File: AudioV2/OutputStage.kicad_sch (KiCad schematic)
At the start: 6 parts, among them K1 DEST LINE, K2 DEST PHONE, K3 DEST MUTE, U1 ULN spare/TODO

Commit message: AudioV2: embed lib_symbols on all child schematics (KiCad 10)
ControlPanel, RelayBoard, and OutputStage had empty lib_symbols and
legacy symbol_inst without pin UUIDs — same pads-only issue as PowerModule.

- Extend sch_helpers: SYMBOL_SOURCES aliases, auto pin_numbers_for,
  BP5293 from Audio/, sanitize (type solid), sub-symbol rename on alias
- Regenerate all sheets via wire_circuit_design.py (power/control/relay/output)
- Fix Pico lib_id to MCU_Module:RaspberryPi_Pico (KiCad 10 name)
- SSD1306-128x64 embeds ER_OLEDM0.91 graphic under alias name
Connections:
- new net: K1.3, K2.10
- new net: K2.3, K3.10
- new net: K1.7, K3.1
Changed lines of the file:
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@@
 		(at 88.9 50.8 0)
 		(unit 1)
+		(body_style 1)
 		(exclude_from_sim no)
 		(in_bom yes)
 		(on_board yes)
+		(in_pos_files yes)
 		(dnp no)
 		(fields_autoplaced yes)
@@
 			)
 		)
-		(property "Description" "AudioV2 draft placeholder"
-			(at 0 0 0)
-			(show_name no)
-			(do_not_autoplace no)
-			(hide yes)
-			(effects
-				(font
-					(size 1.27 1.27)
-				)
-			)
+		(property "Description" ""
+			(at 0 0 0)
+			(show_name no)
+			(do_not_autoplace no)
+			(hide yes)
+			(effects
+				(font
+					(size 1.27 1.27)
+				)
+			)
+		)
+		(pin "1"
+		)
+		(pin "2"
+		)
+		(pin "3"
+		)
+		(pin "4"
+		)
+		(pin "5"
+		)
+		(pin "6"
+		)
+		(pin "7"
+		)
+		(pin "8"
+		)
+		(pin "9"
+		)
+		(pin "10"
 		)
 		(instances
@@
 		(at 101.6 50.8 0)
 		(unit 1)
+		(body_style 1)
 		(exclude_from_sim no)
 		(in_bom yes)
 		(on_board yes)
+		(in_pos_files yes)
 		(dnp no)
 		(fields_autoplaced yes)
@@
 			)
 		)
-		(property "Description" "AudioV2 draft placeholder"
-			(at 0 0 0)
-			(show_name no)
-			(do_not_autoplace no)
-			(hide yes)
-			(effects
-				(font
-					(size 1.27 1.27)
-				)
-			)
+		(property "Description" ""
+			(at 0 0 0)
+			(show_name no)
+			(do_not_autoplace no)
+			(hide yes)
+			(effects
+				(font
+					(size 1.27 1.27)
+				)
+			)
+		)
+		(pin "1"
+		)
+		(pin "2"
+		)
+		(pin "3"
+		)
+		(pin "4"
+		)
+		(pin "5"
+		)
+		(pin "6"
+		)
+		(pin "7"
+		)
+		(pin "8"
+		)
+		(pin "9"
+		)
+		(pin "10"
 		)
 		(instances
@@
 		(at 114.3 50.8 0)
 		(unit 1)
+		(body_style 1)
 		(exclude_from_sim no)
 		(in_bom yes)
 		(on_board yes)
+		(in_pos_files yes)
 		(dnp no)
 		(fields_autoplaced yes)
@@
 			)
 		)
-		(property "Description" "AudioV2 draft placeholder"
-			(at 0 0 0)
-			(show_name no)
-			(do_not_autoplace no)
-			(hide yes)
-			(effects
-				(font
-					(size 1.27 1.27)
-				)
-			)
+		(property "Description" ""
+			(at 0 0 0)
+			(show_name no)
+			(do_not_autoplace no)
+			(hide yes)
+			(effects
+				(font
+					(size 1.27 1.27)
+				)
+			)
+		)
+		(pin "1"
+		)
+		(pin "2"
+		)
+		(pin "3"
+		)
+		(pin "4"
+		)
+		(pin "5"
+		)
+		(pin "6"
+		)
+		(pin "7"
+		)
+		(pin "8"
+		)
+		(pin "9"
+		)
+		(pin "10"
 		)
 		(instances
@@
 		(at 63.5 50.8 0)
 		(unit 1)
+		(body_style 1)
 		(exclude_from_sim no)
 		(in_bom yes)
 		(on_board yes)
+		(in_pos_files yes)
 		(dnp no)
 		(fields_autoplaced yes)
@@
 			)
 		)
-		(property "Description" "AudioV2 draft placeholder"
-			(at 0 0 0)
-			(show_name no)
-			(do_not_autoplace no)
-			(hide yes)
-			(effects
-				(font
-					(size 1.27 1.27)
-				)
-			)
+		(property "Description" ""
+			(at 0 0 0)
+			(show_name no)
+			(do_not_autoplace no)
+			(hide yes)
+			(effects
+				(font
+					(size 1.27 1.27)
+				)
+			)
+		)
+		(pin "1"
+		)
+		(pin "2"
+		)
+		(pin "3"
+		)
+		(pin "4"
+		)
+		(pin "5"
+		)
+		(pin "6"
+		)
+		(pin "7"
+		)
+		(pin "8"
+		)
+		(pin "9"
+		)
+		(pin "10"
+		)
+		(pin "11"
+		)
+		(pin "12"
+		)
+		(pin "13"
+		)
+		(pin "14"
+		)
+		(pin "15"
+		)
+		(pin "16"
+		)
+		(pin "17"
+		)
+		(pin "18"
 		)
 		(instances
@@
 		(at 165.1 45.72 0)
 		(unit 1)
+		(body_style 1)
 		(exclude_from_sim no)
 		(in_bom yes)
 		(on_board yes)
+		(in_pos_files yes)
 		(dnp no)
 		(fields_autoplaced yes)
@@
 			)
 		)
-		(property "Description" "AudioV2 draft placeholder"
-			(at 0 0 0)
-			(show_name no)
-			(do_not_autoplace no)
-			(hide yes)
-			(effects
-				(font
-					(size 1.27 1.27)
-				)
-			)
+		(property "Description" ""
+			(at 0 0 0)
+			(show_name no)
+			(do_not_autoplace no)
+			(hide yes)
+			(effects
+				(font
+					(size 1.27 1.27)
+				)
+			)
+		)
+		(pin "1"
+		)
+		(pin "2"
 		)
 		(instances
@@
 		(at 165.1 50.8 0)
 		(unit 1)
+		(body_style 1)
 		(exclude_from_sim no)
 		(in_bom yes)
 		(on_board yes)
+		(in_pos_files yes)
 		(dnp no)
 		(fields_autoplaced yes)
@@
 			)
 		)
-		(property "Description" "AudioV2 draft placeholder"
-			(at 0 0 0)
-			(show_name no)
-			(do_not_autoplace no)
-			(hide yes)
-			(effects
-				(font
-					(size 1.27 1.27)
-				)
-			)
+		(property "Description" ""
+			(at 0 0 0)
+			(show_name no)
+			(do_not_autoplace no)
+			(hide yes)
+			(effects
+				(font
+					(size 1.27 1.27)
+				)
+			)
+		)
+		(pin "1"
+		)
+		(pin "2"
 		)
 		(instances

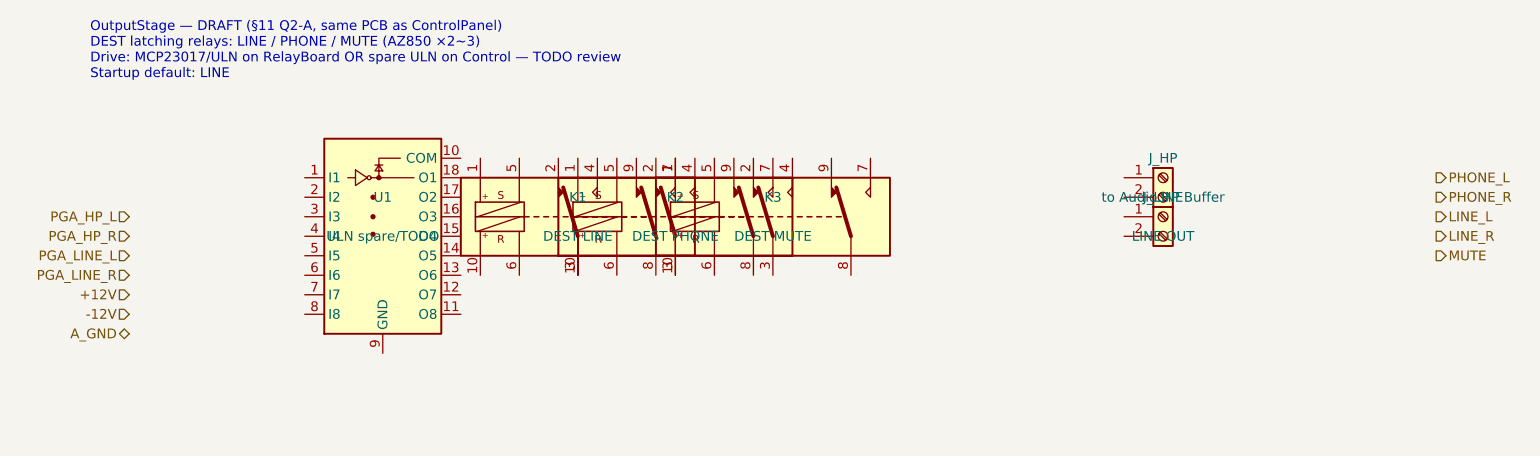
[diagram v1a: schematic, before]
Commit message: feat(AudioV2): 手回し音量構成へ回路図を改訂
- PT2314 を Princeton DS どおり 28pin DIP シンボルに再作成
- PGA2310 / DEST ラッチング / ENC×6 を削除
- OutputStage: SW_DP3T + A50k Dual×2（AMP_SEL→PHONE/LINE）
- ControlPanel: ENC×3 + DEST ラダー(10k/10k/1k) + LED
- CIRCUIT_DESIGN.md を DS 照合・手回し方針に更新
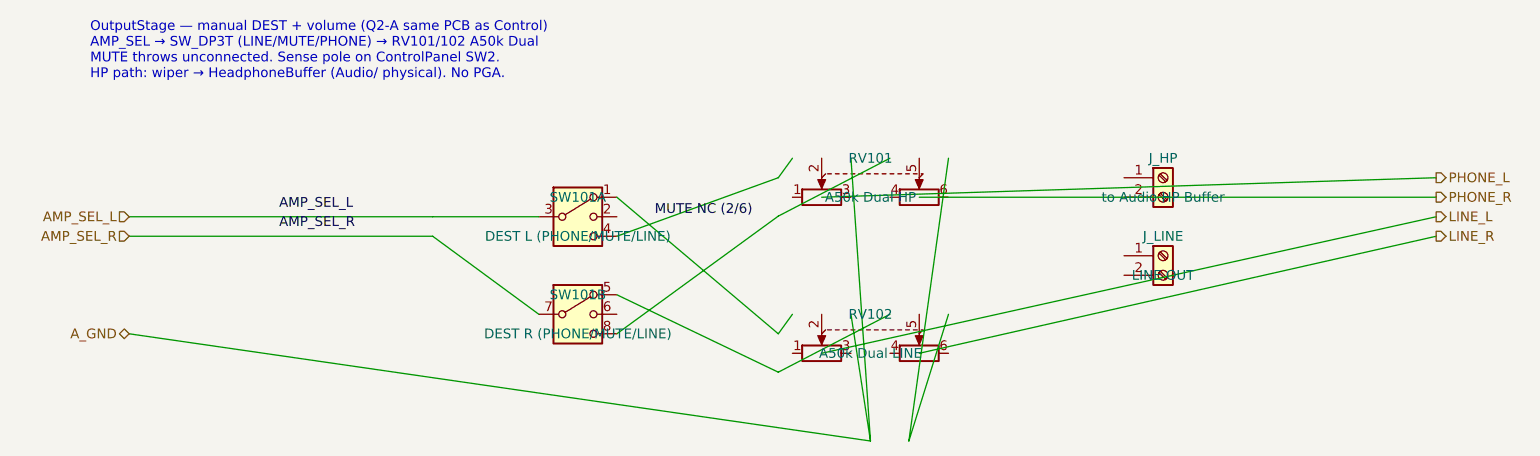
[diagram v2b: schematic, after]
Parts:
- removed K1: DEST LINE, symbol Relay:AZ850P2-x
- removed K2: DEST PHONE, symbol Relay:AZ850P2-x
- removed K3: DEST MUTE, symbol Relay:AZ850P2-x
- removed U1: ULN spare/TODO, symbol Transistor_Array:ULN2803A
- added RV101: A50k Dual HP, symbol Device:R_Potentiometer_Dual
- added RV102: A50k Dual LINE, symbol Device:R_Potentiometer_Dual
- added SW101: DEST L (PHONE/MUTE/LINE), symbol Switch:SW_DP3T
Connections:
- new net AMP_SEL_L: SW101.3
- new net AMP_SEL_R: SW101.7
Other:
- note added: "OutputStage — manual DEST + volume (Q2-A same PCB as Control) AMP_SEL → SW_DP3T (LINE/MUTE/PHONE) → RV101/102 A50k Dual MUTE throws unconnected. Sense pole on ControlPanel SW2. HP path: wiper → HeadphoneBuffer (Audio/ physical). No PGA."
- note removed: "OutputStage — DRAFT (§11 Q2-A, same PCB as ControlPanel) DEST latching relays: LINE / PHONE / MUTE (AZ850 ×2~3) Drive: MCP23017/ULN on RelayBoard OR spare ULN on Control — TODO review Startup default: LINE"

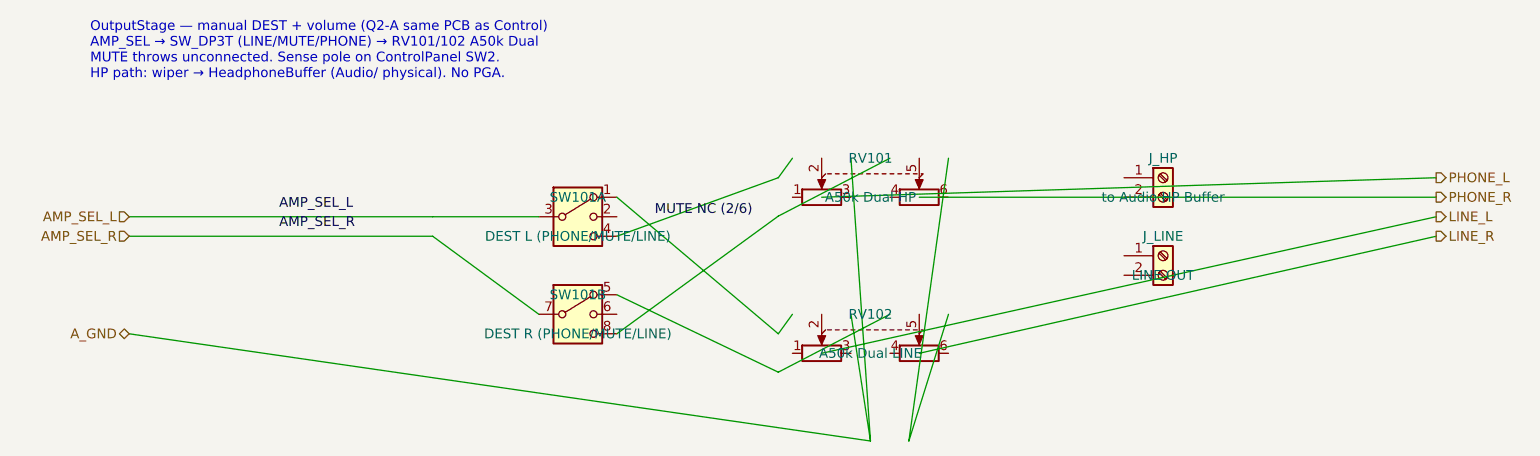
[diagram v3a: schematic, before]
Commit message: AudioV2: ラベル結線で Power/Control/Output をネット接続
pin_connect を tip=(at) 基準に修正し、同名ローカルラベルをピン tip に
載せて結線。グリッドスナップ一致・パッシブ間隔・親シートピン橋渡しを
整え、一次 PD_GND と二次 A_GND の分離を維持。
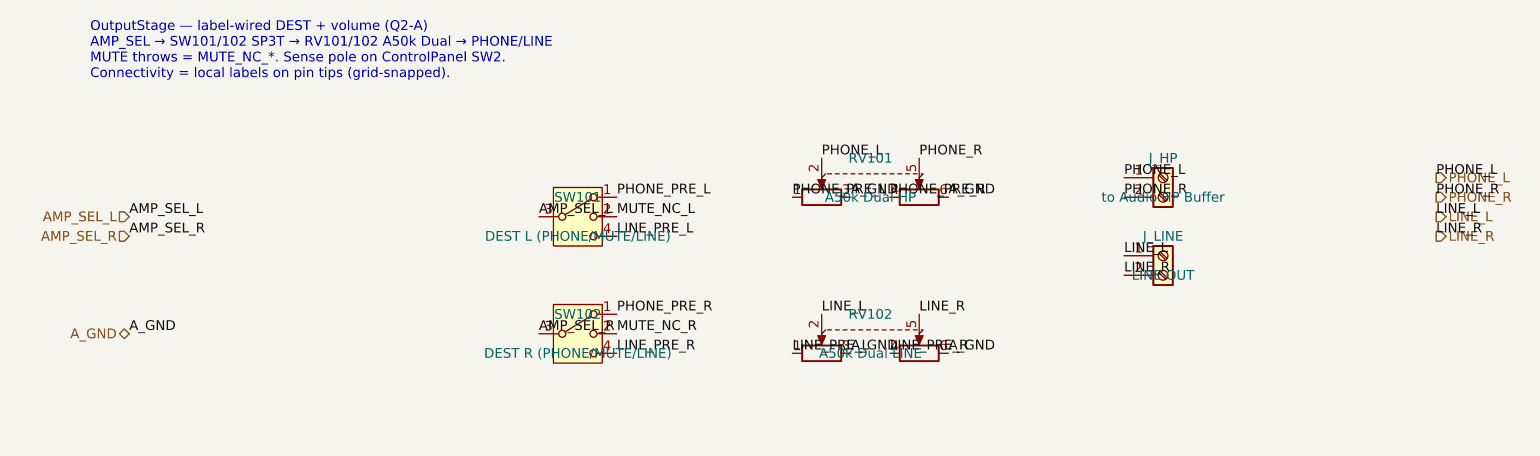
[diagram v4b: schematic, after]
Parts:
- removed SW101: DEST L (PHONE/MUTE/LINE), symbol Switch:SW_DP3T
- added SW101: DEST L (PHONE/MUTE/LINE), symbol Switch:SW_SP3T
- added SW102: DEST R (PHONE/MUTE/LINE), symbol Switch:SW_SP3T
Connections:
- net AMP_SEL_L: now also SW101.3
- net AMP_SEL_R: now also SW102.3
- net A_GND: now also RV101.3, RV101.6, RV102.3, RV102.6
- net LINE_L: now also J_LINE.1 (Pin_1), RV102.2
- net LINE_R: now also J_LINE.2 (Pin_2), RV102.5
- net PHONE_L: now also J_HP.1 (Pin_1), RV101.2
- net PHONE_R: now also J_HP.2 (Pin_2), RV101.5
- net LINE_PRE_L: now reaches RV102.1
- net LINE_PRE_L: now also SW101.4
- net LINE_PRE_R: now reaches RV102.4
- net LINE_PRE_R: now also SW102.4
- net PHONE_PRE_L: now reaches RV101.1
- net PHONE_PRE_L: now also SW101.1
- net PHONE_PRE_R: now reaches RV101.4
- net PHONE_PRE_R: now also SW102.1
- new net MUTE_NC_L: SW101.2
- new net MUTE_NC_R: SW102.2
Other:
- note added: "OutputStage — label-wired DEST + volume (Q2-A) AMP_SEL → SW101/102 SP3T → RV101/102 A50k Dual → PHONE/LINE MUTE throws = MUTE_NC_*. Sense pole on ControlPanel SW2. Connectivity = local labels on pin tips (grid-snapped)."
- note removed: "OutputStage — manual DEST + volume (Q2-A same PCB as Control) AMP_SEL → SW_DP3T (LINE/MUTE/PHONE) → RV101/102 A50k Dual MUTE throws unconnected. Sense pole on ControlPanel SW2. HP path: wiper → HeadphoneBuffer (Audio/ physical). No PGA."
